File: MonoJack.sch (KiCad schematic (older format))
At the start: 3 parts

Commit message: got the schematic done
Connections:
- net G_GND renamed GND
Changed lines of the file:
@@
 $Descr A4 11693 8268
 encoding utf-8
-Sheet 3 9
+Sheet 8 14
 Title ""
 Date ""
@@
 AR Path="/5FBCFD33/5FC24699/5FC1DE1B" Ref="J?"  Part="1"
 AR Path="/5FBCFD33/5FC2469C/5FC1DE1B" Ref="J?"  Part="1"
+AR Path="/5FC42267/5FC5ED5A/5FC1DE1B" Ref="J?"  Part="1"
+AR Path="/5FC42267/5FC5ED5D/5FC1DE1B" Ref="J?"  Part="1"
+AR Path="/5FC42267/5FC5ED60/5FC1DE1B" Ref="J?"  Part="1"
 F 0 "J?" H 4150 3615 50  0000 C CNN
 F 1 "6.35mmMonoAudioJack" H 4150 3524 50  0000 C CNN
@@
 	1    0    0    -1
 $EndComp
-Text GLabel 3900 4350 3    50   Input ~ 0
-G_GND
 Wire Wire Line
 	3900 4150 3900 4350
@@
 AR Path="/5FBCFD33/5FC24699/5FC1F9CC" Ref="J?"  Part="1"
 AR Path="/5FBCFD33/5FC2469C/5FC1F9CC" Ref="J?"  Part="1"
+AR Path="/5FC42267/5FC5ED5A/5FC1F9CC" Ref="J?"  Part="1"
+AR Path="/5FC42267/5FC5ED5D/5FC1F9CC" Ref="J?"  Part="1"
+AR Path="/5FC42267/5FC5ED60/5FC1F9CC" Ref="J?"  Part="1"
 F 0 "J?" V 4488 3212 50  0000 R CNN
 F 1 "Conn_01x02_Female" V 4397 3212 50  0000 R CNN
@@
 AR Path="/5FBCFD33/5FC24699/5FC215E5" Ref="R?"  Part="1"
 AR Path="/5FBCFD33/5FC2469C/5FC215E5" Ref="R?"  Part="1"
+AR Path="/5FC42267/5FC5ED5A/5FC215E5" Ref="R?"  Part="1"
+AR Path="/5FC42267/5FC5ED5D/5FC215E5" Ref="R?"  Part="1"
+AR Path="/5FC42267/5FC5ED60/5FC215E5" Ref="R?"  Part="1"
 F 0 "R?" V 3843 4150 50  0000 C CNN
 F 1 "optional R" V 3934 4150 50  0000 C CNN
@@
 Wire Wire Line
 	4650 4150 4200 4150
+$Comp
+L power:GND #PWR?
+U 1 1 5FBEFFFB
+P 3900 4350
+F 0 "#PWR?" H 3900 4100 50  0001 C CNN
+F 1 "GND" H 3905 4177 50  0000 C CNN
+F 2 "" H 3900 4350 50  0001 C CNN
+F 3 "" H 3900 4350 50  0001 C CNN
+	1    3900 4350
+	1    0    0    -1
+$EndComp
 $EndSCHEMATC

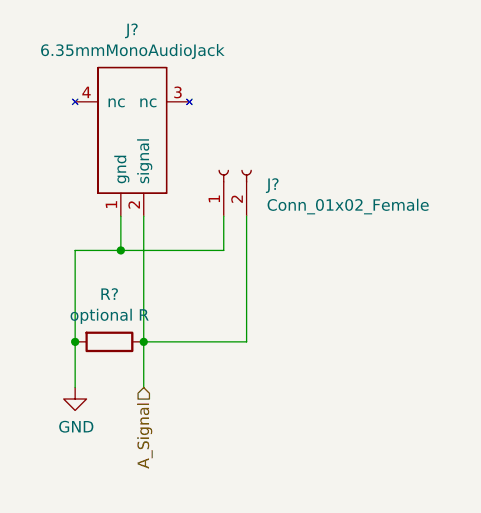
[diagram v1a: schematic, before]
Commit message: added the needed footprints
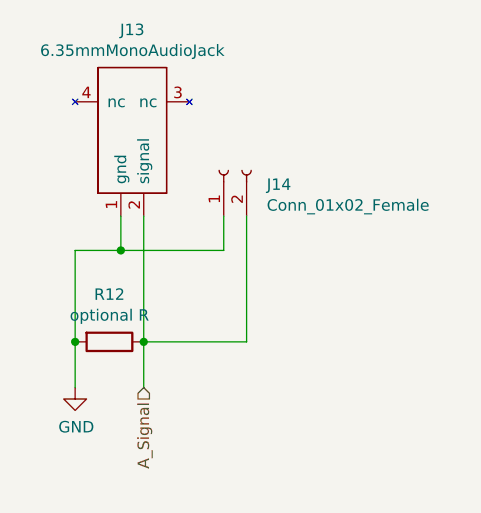
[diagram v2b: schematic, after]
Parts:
- J19: renamed from J?; footprint (none) -> LocalFootPrints:6.35mmMonoAudioJack
- J20: renamed from J?; footprint (none) -> Connector_PinHeader_2.54mm:PinHeader_1x02_P2.54mm_Vertical
- R15: renamed from R?; footprint (none) -> Resistor_THT:R_Axial_DIN0207_L6.3mm_D2.5mm_P7.62mm_Horizontal
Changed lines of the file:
@@
 $Descr A4 11693 8268
 encoding utf-8
-Sheet 8 14
+Sheet 5 14
 Title ""
 Date ""
@@
 $EndDescr
 $Comp
-L NewSymbols:6.35mmMonoAudioJack J?
+L NewSymbols:6.35mmMonoAudioJack J19
 U 1 1 5FC1DE1B
 P 4150 3200
-AR Path="/5FBCFD33/5FC1DA06/5FC1DE1B" Ref="J?"  Part="1"
-AR Path="/5FBCFD33/5FC22BEB/5FC1DE1B" Ref="J?"  Part="1"
-AR Path="/5FBCFD33/5FC22EFE/5FC1DE1B" Ref="J?"  Part="1"
-AR Path="/5FBCFD33/5FC22F36/5FC1DE1B" Ref="J?"  Part="1"
-AR Path="/5FBCFD33/5FC22FFE/5FC1DE1B" Ref="J?"  Part="1"
-AR Path="/5FBCFD33/5FC230D2/5FC1DE1B" Ref="J?"  Part="1"
-AR Path="/5FBCFD33/5FC231A0/5FC1DE1B" Ref="J?"  Part="1"
-AR Path="/5FBCFD33/5FC24696/5FC1DE1B" Ref="J?"  Part="1"
-AR Path="/5FBCFD33/5FC24699/5FC1DE1B" Ref="J?"  Part="1"
-AR Path="/5FBCFD33/5FC2469C/5FC1DE1B" Ref="J?"  Part="1"
+AR Path="/5FBCFD33/5FC1DA06/5FC1DE1B" Ref="J19"  Part="1"
+AR Path="/5FBCFD33/5FC22BEB/5FC1DE1B" Ref="J17"  Part="1"
+AR Path="/5FBCFD33/5FC22EFE/5FC1DE1B" Ref="J15"  Part="1"
+AR Path="/5FBCFD33/5FC22F36/5FC1DE1B" Ref="J13"  Part="1"
+AR Path="/5FBCFD33/5FC22FFE/5FC1DE1B" Ref="J21"  Part="1"
+AR Path="/5FBCFD33/5FC230D2/5FC1DE1B" Ref="J23"  Part="1"
+AR Path="/5FBCFD33/5FC231A0/5FC1DE1B" Ref="J25"  Part="1"
+AR Path="/5FBCFD33/5FC24696/5FC1DE1B" Ref="J27"  Part="1"
+AR Path="/5FBCFD33/5FC24699/5FC1DE1B" Ref="J29"  Part="1"
+AR Path="/5FBCFD33/5FC2469C/5FC1DE1B" Ref="J31"  Part="1"
 AR Path="/5FC42267/5FC5ED5A/5FC1DE1B" Ref="J?"  Part="1"
 AR Path="/5FC42267/5FC5ED5D/5FC1DE1B" Ref="J?"  Part="1"
 AR Path="/5FC42267/5FC5ED60/5FC1DE1B" Ref="J?"  Part="1"
-F 0 "J?" H 4150 3615 50  0000 C CNN
+F 0 "J13" H 4150 3615 50  0000 C CNN
 F 1 "6.35mmMonoAudioJack" H 4150 3524 50  0000 C CNN
-F 2 "" H 4000 3650 50  0001 C CNN
+F 2 "LocalFootPrints:6.35mmMonoAudioJack" H 4000 3650 50  0001 C CNN
 F 3 "" H 4000 3650 50  0001 C CNN
 	1    4150 3200
@@
 	4200 4350 4200 4150
 $Comp
-L Connector:Conn_01x02_Female J?
+L Connector:Conn_01x02_Female J20
 U 1 1 5FC1F9CC
 P 4550 3400
-AR Path="/5FBCFD33/5FC1DA06/5FC1F9CC" Ref="J?"  Part="1"
-AR Path="/5FBCFD33/5FC22BEB/5FC1F9CC" Ref="J?"  Part="1"
-AR Path="/5FBCFD33/5FC22EFE/5FC1F9CC" Ref="J?"  Part="1"
-AR Path="/5FBCFD33/5FC22F36/5FC1F9CC" Ref="J?"  Part="1"
-AR Path="/5FBCFD33/5FC22FFE/5FC1F9CC" Ref="J?"  Part="1"
-AR Path="/5FBCFD33/5FC230D2/5FC1F9CC" Ref="J?"  Part="1"
-AR Path="/5FBCFD33/5FC231A0/5FC1F9CC" Ref="J?"  Part="1"
-AR Path="/5FBCFD33/5FC24696/5FC1F9CC" Ref="J?"  Part="1"
-AR Path="/5FBCFD33/5FC24699/5FC1F9CC" Ref="J?"  Part="1"
-AR Path="/5FBCFD33/5FC2469C/5FC1F9CC" Ref="J?"  Part="1"
+AR Path="/5FBCFD33/5FC1DA06/5FC1F9CC" Ref="J20"  Part="1"
+AR Path="/5FBCFD33/5FC22BEB/5FC1F9CC" Ref="J18"  Part="1"
+AR Path="/5FBCFD33/5FC22EFE/5FC1F9CC" Ref="J16"  Part="1"
+AR Path="/5FBCFD33/5FC22F36/5FC1F9CC" Ref="J14"  Part="1"
+AR Path="/5FBCFD33/5FC22FFE/5FC1F9CC" Ref="J22"  Part="1"
+AR Path="/5FBCFD33/5FC230D2/5FC1F9CC" Ref="J24"  Part="1"
+AR Path="/5FBCFD33/5FC231A0/5FC1F9CC" Ref="J26"  Part="1"
+AR Path="/5FBCFD33/5FC24696/5FC1F9CC" Ref="J28"  Part="1"
+AR Path="/5FBCFD33/5FC24699/5FC1F9CC" Ref="J30"  Part="1"
+AR Path="/5FBCFD33/5FC2469C/5FC1F9CC" Ref="J32"  Part="1"
 AR Path="/5FC42267/5FC5ED5A/5FC1F9CC" Ref="J?"  Part="1"
 AR Path="/5FC42267/5FC5ED5D/5FC1F9CC" Ref="J?"  Part="1"
 AR Path="/5FC42267/5FC5ED60/5FC1F9CC" Ref="J?"  Part="1"
-F 0 "J?" V 4488 3212 50  0000 R CNN
+F 0 "J14" V 4488 3212 50  0000 R CNN
 F 1 "Conn_01x02_Female" V 4397 3212 50  0000 R CNN
-F 2 "" H 4550 3400 50  0001 C CNN
+F 2 "Connector_PinHeader_2.54mm:PinHeader_1x02_P2.54mm_Vertical" H 4550 3400 50  0001 C CNN
 F 3 "~" H 4550 3400 50  0001 C CNN
 	1    4550 3400
@@
 $EndComp
 $Comp
-L Device:R R?
+L Device:R R15
 U 1 1 5FC215E5
 P 4050 4150
-AR Path="/5FBCFD33/5FC1DA06/5FC215E5" Ref="R?"  Part="1"
-AR Path="/5FBCFD33/5FC22BEB/5FC215E5" Ref="R?"  Part="1"
-AR Path="/5FBCFD33/5FC22EFE/5FC215E5" Ref="R?"  Part="1"
-AR Path="/5FBCFD33/5FC22F36/5FC215E5" Ref="R?"  Part="1"
-AR Path="/5FBCFD33/5FC22FFE/5FC215E5" Ref="R?"  Part="1"
-AR Path="/5FBCFD33/5FC230D2/5FC215E5" Ref="R?"  Part="1"
-AR Path="/5FBCFD33/5FC231A0/5FC215E5" Ref="R?"  Part="1"
-AR Path="/5FBCFD33/5FC24696/5FC215E5" Ref="R?"  Part="1"
-AR Path="/5FBCFD33/5FC24699/5FC215E5" Ref="R?"  Part="1"
-AR Path="/5FBCFD33/5FC2469C/5FC215E5" Ref="R?"  Part="1"
+AR Path="/5FBCFD33/5FC1DA06/5FC215E5" Ref="R15"  Part="1"
+AR Path="/5FBCFD33/5FC22BEB/5FC215E5" Ref="R14"  Part="1"
+AR Path="/5FBCFD33/5FC22EFE/5FC215E5" Ref="R13"  Part="1"
+AR Path="/5FBCFD33/5FC22F36/5FC215E5" Ref="R12"  Part="1"
+AR Path="/5FBCFD33/5FC22FFE/5FC215E5" Ref="R16"  Part="1"
+AR Path="/5FBCFD33/5FC230D2/5FC215E5" Ref="R17"  Part="1"
+AR Path="/5FBCFD33/5FC231A0/5FC215E5" Ref="R18"  Part="1"
+AR Path="/5FBCFD33/5FC24696/5FC215E5" Ref="R19"  Part="1"
+AR Path="/5FBCFD33/5FC24699/5FC215E5" Ref="R20"  Part="1"
+AR Path="/5FBCFD33/5FC2469C/5FC215E5" Ref="R21"  Part="1"
 AR Path="/5FC42267/5FC5ED5A/5FC215E5" Ref="R?"  Part="1"
 AR Path="/5FC42267/5FC5ED5D/5FC215E5" Ref="R?"  Part="1"
 AR Path="/5FC42267/5FC5ED60/5FC215E5" Ref="R?"  Part="1"
-F 0 "R?" V 3843 4150 50  0000 C CNN
+F 0 "R12" V 3843 4150 50  0000 C CNN
 F 1 "optional R" V 3934 4150 50  0000 C CNN
-F 2 "" V 3980 4150 50  0001 C CNN
+F 2 "Resistor_THT:R_Axial_DIN0207_L6.3mm_D2.5mm_P7.62mm_Horizontal" V 3980 4150 50  0001 C CNN
 F 3 "~" H 4050 4150 50  0001 C CNN
 	1    4050 4150
@@
 	4650 4150 4200 4150
 $Comp
-L power:GND #PWR?
+L power:GND #PWR036
 U 1 1 5FBEFFFB
 P 3900 4350
-F 0 "#PWR?" H 3900 4100 50  0001 C CNN
+AR Path="/5FBCFD33/5FC1DA06/5FBEFFFB" Ref="#PWR036"  Part="1"
+AR Path="/5FBCFD33/5FC22F36/5FBEFFFB" Ref="#PWR033"  Part="1"
+AR Path="/5FBCFD33/5FC22EFE/5FBEFFFB" Ref="#PWR034"  Part="1"
+AR Path="/5FBCFD33/5FC22BEB/5FBEFFFB" Ref="#PWR035"  Part="1"
+AR Path="/5FBCFD33/5FC22FFE/5FBEFFFB" Ref="#PWR037"  Part="1"
+AR Path="/5FBCFD33/5FC230D2/5FBEFFFB" Ref="#PWR038"  Part="1"
+AR Path="/5FBCFD33/5FC231A0/5FBEFFFB" Ref="#PWR039"  Part="1"
+AR Path="/5FBCFD33/5FC24696/5FBEFFFB" Ref="#PWR040"  Part="1"
+AR Path="/5FBCFD33/5FC24699/5FBEFFFB" Ref="#PWR041"  Part="1"
+AR Path="/5FBCFD33/5FC2469C/5FBEFFFB" Ref="#PWR042"  Part="1"
+F 0 "#PWR033" H 3900 4100 50  0001 C CNN
 F 1 "GND" H 3905 4177 50  0000 C CNN
 F 2 "" H 3900 4350 50  0001 C CNN

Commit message: layout time
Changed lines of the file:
@@
 $Descr A4 11693 8268
 encoding utf-8
-Sheet 5 14
+Sheet 6 14
 Title ""
 Date ""
@@
 AR Path="/5FC42267/5FC5ED5D/5FC1DE1B" Ref="J?"  Part="1"
 AR Path="/5FC42267/5FC5ED60/5FC1DE1B" Ref="J?"  Part="1"
-F 0 "J13" H 4150 3615 50  0000 C CNN
+F 0 "J15" H 4150 3615 50  0000 C CNN
 F 1 "6.35mmMonoAudioJack" H 4150 3524 50  0000 C CNN
 F 2 "LocalFootPrints:6.35mmMonoAudioJack" H 4000 3650 50  0001 C CNN
@@
 AR Path="/5FC42267/5FC5ED5D/5FC1F9CC" Ref="J?"  Part="1"
 AR Path="/5FC42267/5FC5ED60/5FC1F9CC" Ref="J?"  Part="1"
-F 0 "J14" V 4488 3212 50  0000 R CNN
+F 0 "J16" V 4488 3212 50  0000 R CNN
 F 1 "Conn_01x02_Female" V 4397 3212 50  0000 R CNN
 F 2 "Connector_PinHeader_2.54mm:PinHeader_1x02_P2.54mm_Vertical" H 4550 3400 50  0001 C CNN
@@
 AR Path="/5FC42267/5FC5ED5D/5FC215E5" Ref="R?"  Part="1"
 AR Path="/5FC42267/5FC5ED60/5FC215E5" Ref="R?"  Part="1"
-F 0 "R12" V 3843 4150 50  0000 C CNN
+F 0 "R13" V 3843 4150 50  0000 C CNN
 F 1 "optional R" V 3934 4150 50  0000 C CNN
 F 2 "Resistor_THT:R_Axial_DIN0207_L6.3mm_D2.5mm_P7.62mm_Horizontal" V 3980 4150 50  0001 C CNN
@@
 AR Path="/5FBCFD33/5FC24699/5FBEFFFB" Ref="#PWR041"  Part="1"
 AR Path="/5FBCFD33/5FC2469C/5FBEFFFB" Ref="#PWR042"  Part="1"
-F 0 "#PWR033" H 3900 4100 50  0001 C CNN
+F 0 "#PWR034" H 3900 4100 50  0001 C CNN
 F 1 "GND" H 3905 4177 50  0000 C CNN
 F 2 "" H 3900 4350 50  0001 C CNN

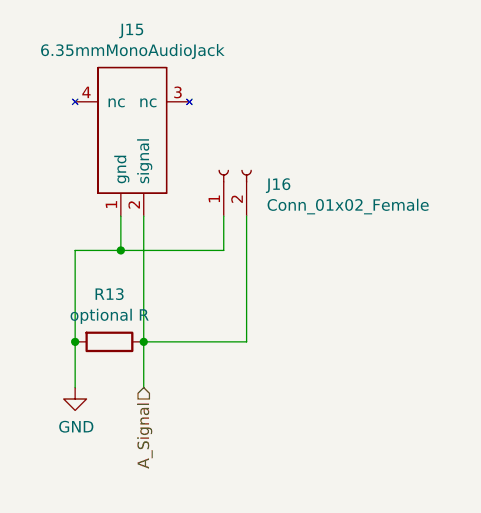
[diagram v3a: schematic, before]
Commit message: added board layout
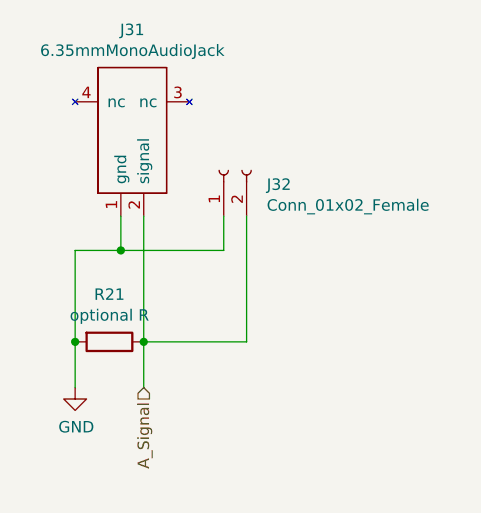
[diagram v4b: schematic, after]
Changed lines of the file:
@@
 AR Path="/5FC42267/5FC5ED5D/5FC1DE1B" Ref="J?"  Part="1"
 AR Path="/5FC42267/5FC5ED60/5FC1DE1B" Ref="J?"  Part="1"
-F 0 "J15" H 4150 3615 50  0000 C CNN
+F 0 "J31" H 4150 3615 50  0000 C CNN
 F 1 "6.35mmMonoAudioJack" H 4150 3524 50  0000 C CNN
 F 2 "LocalFootPrints:6.35mmMonoAudioJack" H 4000 3650 50  0001 C CNN
@@
 AR Path="/5FC42267/5FC5ED5D/5FC1F9CC" Ref="J?"  Part="1"
 AR Path="/5FC42267/5FC5ED60/5FC1F9CC" Ref="J?"  Part="1"
-F 0 "J16" V 4488 3212 50  0000 R CNN
+F 0 "J32" V 4488 3212 50  0000 R CNN
 F 1 "Conn_01x02_Female" V 4397 3212 50  0000 R CNN
 F 2 "Connector_PinHeader_2.54mm:PinHeader_1x02_P2.54mm_Vertical" H 4550 3400 50  0001 C CNN
@@
 AR Path="/5FC42267/5FC5ED5D/5FC215E5" Ref="R?"  Part="1"
 AR Path="/5FC42267/5FC5ED60/5FC215E5" Ref="R?"  Part="1"
-F 0 "R13" V 3843 4150 50  0000 C CNN
+F 0 "R21" V 3843 4150 50  0000 C CNN
 F 1 "optional R" V 3934 4150 50  0000 C CNN
 F 2 "Resistor_THT:R_Axial_DIN0207_L6.3mm_D2.5mm_P7.62mm_Horizontal" V 3980 4150 50  0001 C CNN
@@
 AR Path="/5FBCFD33/5FC24699/5FBEFFFB" Ref="#PWR041"  Part="1"
 AR Path="/5FBCFD33/5FC2469C/5FBEFFFB" Ref="#PWR042"  Part="1"
-F 0 "#PWR034" H 3900 4100 50  0001 C CNN
+F 0 "#PWR042" H 3900 4100 50  0001 C CNN
 F 1 "GND" H 3905 4177 50  0000 C CNN
 F 2 "" H 3900 4350 50  0001 C CNN
